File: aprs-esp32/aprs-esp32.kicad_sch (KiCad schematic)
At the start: 47 parts, among them J1 GPS_CONNECTOR, J2 EXT_1WIRE, J3 PSU_CONN, J4 I2C, J5 M20-6102045, J6 RF_HI_LOW, J7 RF_OUT, J8 ESP PROGRAM, Q1 BSS138, Q2 BSS138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

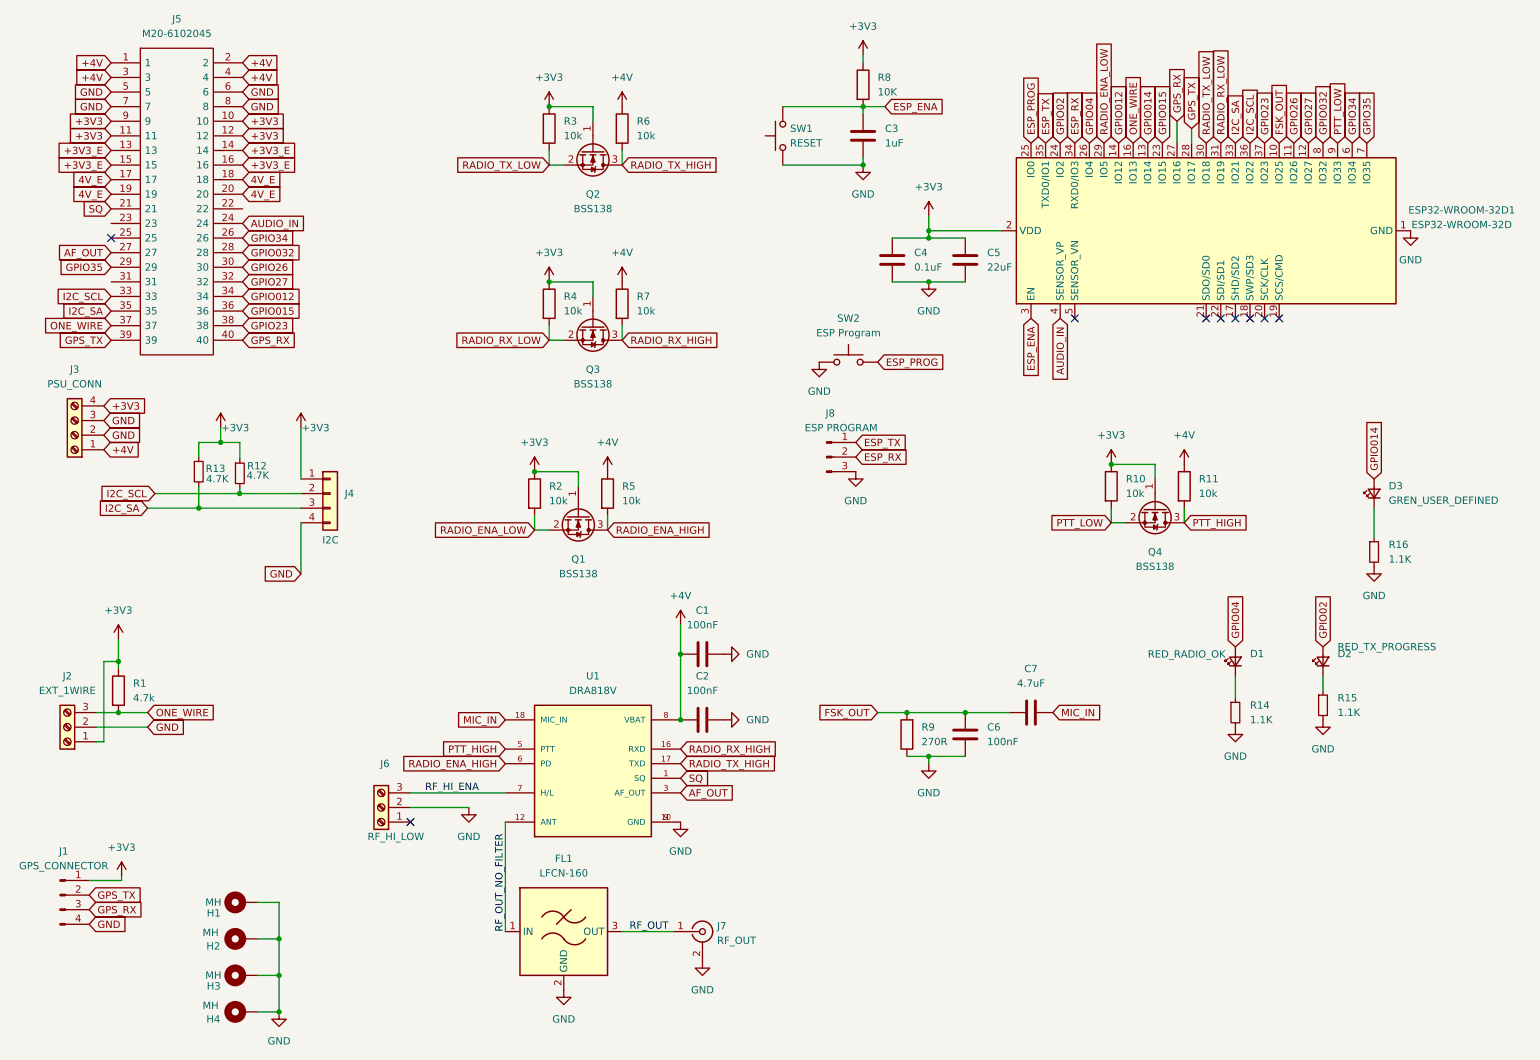
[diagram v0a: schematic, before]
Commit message: limpieza de esquematico
movi los level shifters a su propia pagina
movi la mayor parte de los conectores a una pagina separada
corregido: simbolos de pin desconectado faltantes
cambio: ESP renombrado a u2
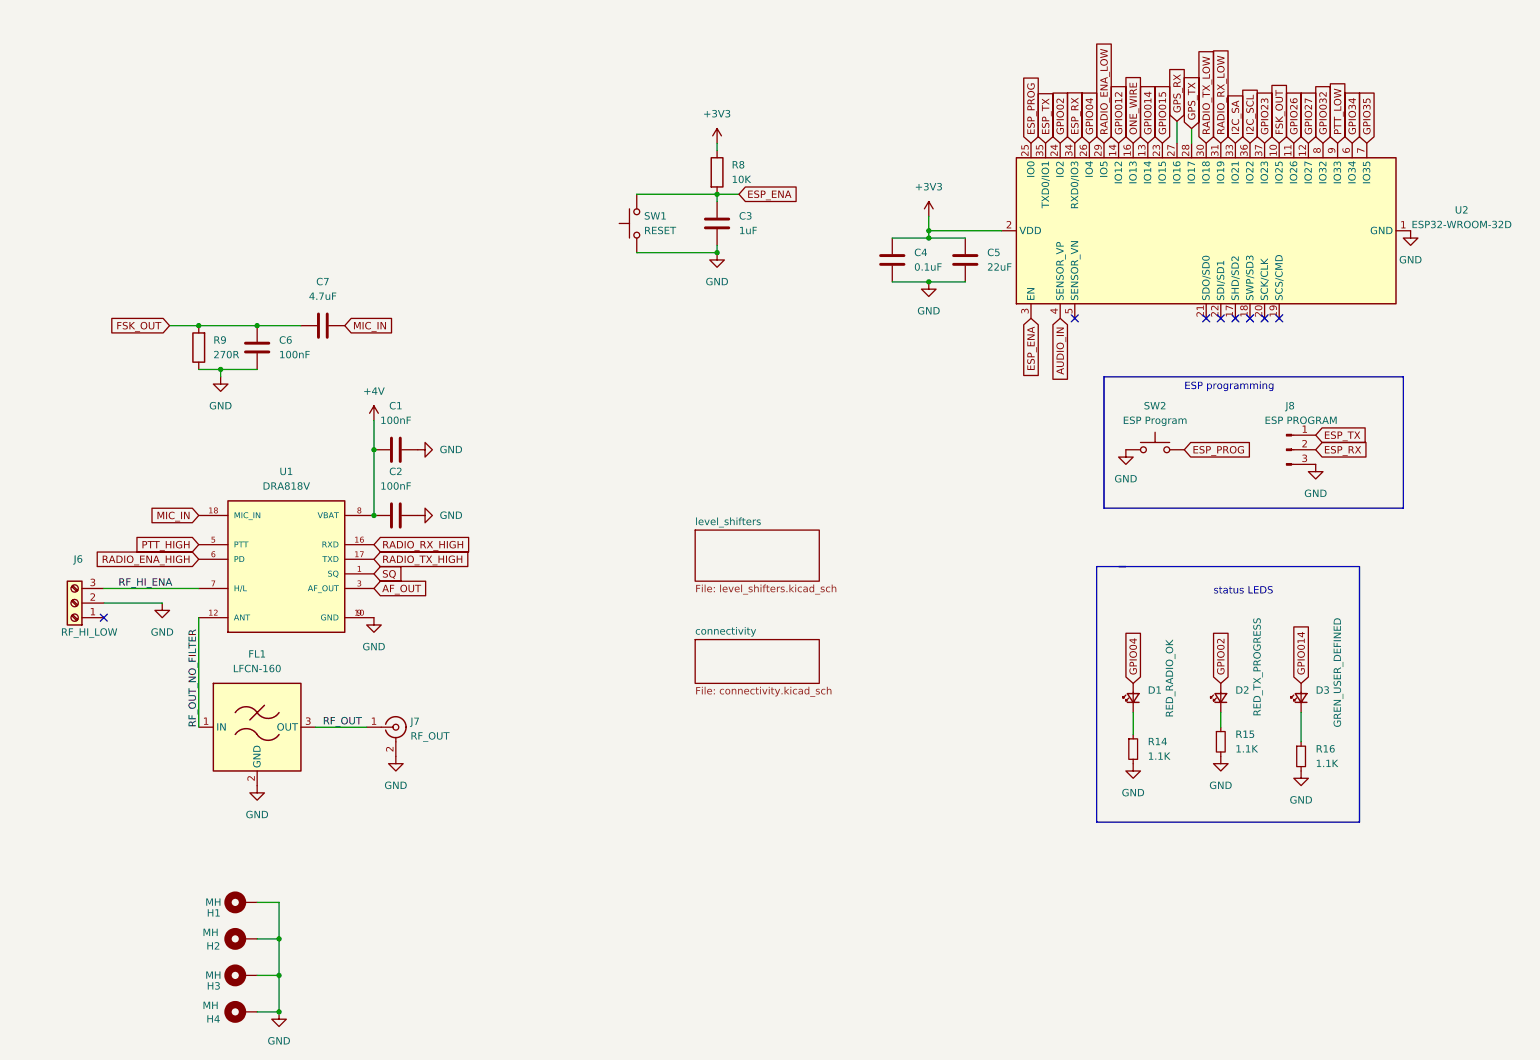
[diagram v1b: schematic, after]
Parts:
- removed J1: GPS_CONNECTOR, Connector_PinHeader_2.54mm:PinHeader_1x04_P2.54mm_Vertical, symbol Connector:Conn_01x04_Male
- removed J2: EXT_1WIRE, Connector_PinHeader_2.54mm:PinHeader_1x03_P2.54mm_Vertical, symbol Connector:Screw_Terminal_01x03
- removed J3: PSU_CONN, TerminalBlock:TerminalBlock_Altech_AK300-4_P5.00mm, symbol Connector:Screw_Terminal_01x04
- removed J4: I2C, Connector_PinHeader_2.54mm:PinHeader_1x04_P2.54mm_Vertical, symbol Connector_Generic:Conn_01x04
- removed J5: M20-6102045, M20-6102045:RHDR40W66P254_2X20_5146X500X1105P, symbol M20-6102045:M20-6102045
- removed Q1, Q2, Q3, Q4: BSS138, Package_TO_SOT_SMD:SOT-23, symbol Transistor_FET:BSS138
- removed R1: 4.7k, Resistor_SMD:R_1206_3216Metric_Pad1.30x1.75mm_HandSolder, symbol Device:R
- removed R10, R11, R2, R3, R4, R5, R6, R7: 10k, Resistor_SMD:R_1206_3216Metric_Pad1.30x1.75mm_HandSolder, symbol Device:R
- removed R12, R13: 4.7K, Resistor_SMD:R_1206_3216Metric_Pad1.30x1.75mm_HandSolder, symbol Device:R_Small
- renumbered ESP32-WROOM-32D1 to U2
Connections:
- no-connect marks 9 -> 8
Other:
- added sheet connectivity (connectivity.kicad_sch)
- added sheet level_shifters (level_shifters.kicad_sch)
- note added: "ESP programming"
- note added: "status LEDS"
- moved on the sheet: C1, C2, C3, C6, C7, D1, D2, D3, FL1, J6, J7, J8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
